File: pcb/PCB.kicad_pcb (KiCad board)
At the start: 4 copper layers, 29.2 x 51.1 mm, 35 parts, among them J1 Conn_01x15, J2 USB_C_Receptacle_USB2.0, J3 Conn_01x15, J4 TC2030, J5 Conn_01x04, SW1 SW_Push, SW2 SW_Push, U1 SN65HVD230, U2 AMS1117-3.3, U3 STM32F103C8T6, Y1 8MHz

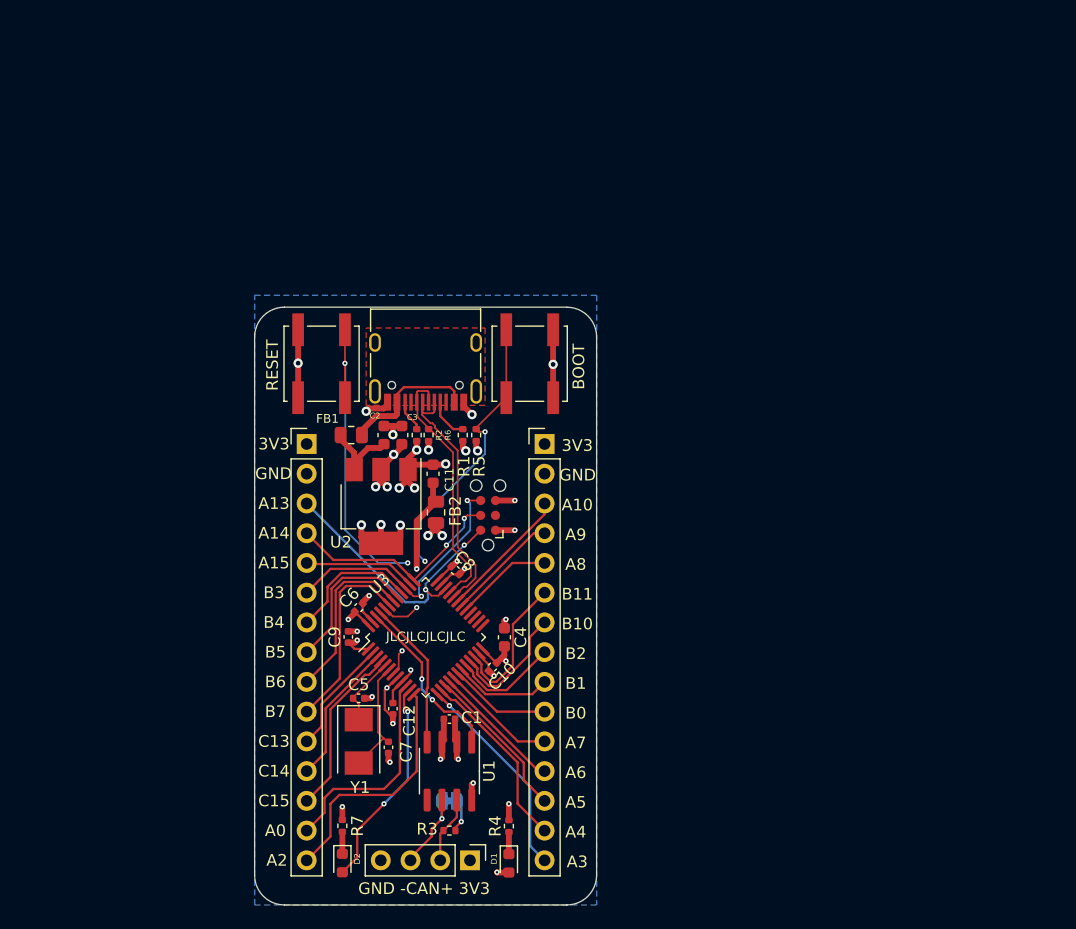
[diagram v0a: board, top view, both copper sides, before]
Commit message: created schematic and layout of the telemetry board
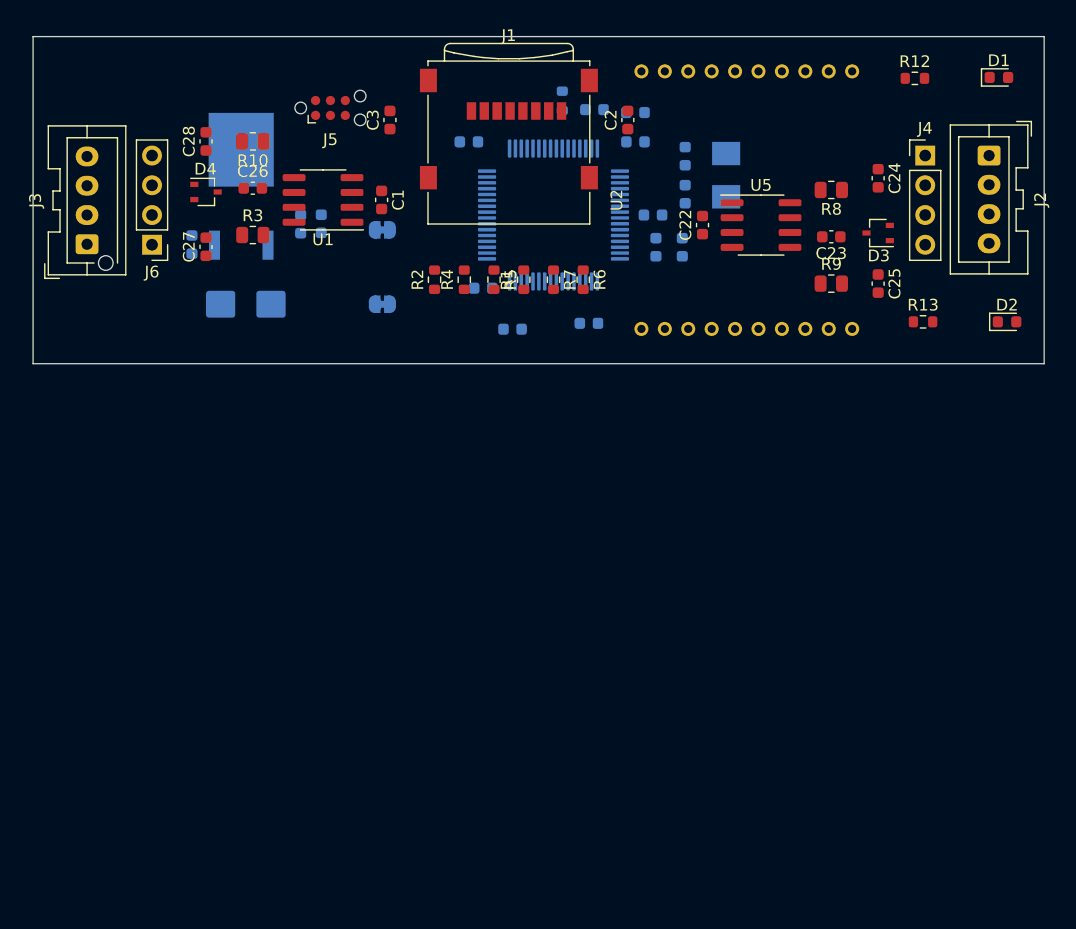
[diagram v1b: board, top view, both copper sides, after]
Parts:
- removed C10, C12, C8, C9: 100n, Capacitor_SMD:C_0402_1005Metric
- removed C11: 1u, Capacitor_SMD:C_0603_1608Metric
- removed C7: 30p, Capacitor_SMD:C_0402_1005Metric
- removed FB1, FB2: 100R@100MHz, Resistor_SMD:R_0805_2012Metric
- removed SW1, SW2: SW_Push, Button_Switch_SMD:SW_Push_1P1T_NO_CK_KSC7xxJ
- removed U3: STM32F103C8T6, Package_QFP:LQFP-48_7x7mm_P0.5mm
- removed Y1: 8MHz, Crystal:Crystal_SMD_5032-2Pin_5.0x3.2mm
- added C13: 4u7, Capacitor_SMD:C_0603_1608Metric, B.Cu at (169.2, 72.1)
- added C14: 100n, Capacitor_SMD:C_0603_1608Metric, B.Cu at (167.0, 72.1)
- added C15: 100n, Capacitor_SMD:C_0603_1608Metric, B.Cu at (161.7, 60.3)
- added C16: 100n, Capacitor_SMD:C_0603_1608Metric, B.Cu at (151.0, 63.1)
- added C17: 100n, Capacitor_SMD:C_0603_1608Metric, B.Cu at (165.2, 63.1)
- added C18: 1u, Capacitor_SMD:C_0603_1608Metric, B.Cu at (165.2, 60.6)
- added C19: 100n, Capacitor_SMD:C_0603_1608Metric, B.Cu at (154.7, 79.1)
- added C20: 4u7, Capacitor_SMD:C_0603_1608Metric, B.Cu at (152.2, 75.6)
- added C21: 100n, Capacitor_SMD:C_0603_1608Metric, B.Cu at (161.3, 78.6)
- added C22: 100n, Capacitor_SMD:C_0603_1608Metric, F.Cu at (171.0, 70.2)
- added C23: 100n, Capacitor_SMD:C_0603_1608Metric, F.Cu at (182.0, 71.2)
- added C24: 30p, Capacitor_SMD:C_0603_1608Metric, F.Cu at (186.0, 66.2)
- added C25: 30p, Capacitor_SMD:C_0603_1608Metric, F.Cu at (186.0, 75.2)
- added C26: 100n, Capacitor_SMD:C_0603_1608Metric, F.Cu at (132.6, 67.1)
- added C27: 30p, Capacitor_SMD:C_0603_1608Metric, F.Cu at (128.6, 72.1)
- added C28: 30p, Capacitor_SMD:C_0603_1608Metric, F.Cu at (128.6, 63.1)
- added C29: 30p, Capacitor_SMD:C_0603_1608Metric, B.Cu at (169.5, 64.3)
- added C30: 30p, Capacitor_SMD:C_0603_1608Metric, B.Cu at (169.5, 67.6)
- added C31: 100n, Capacitor_SMD:C_0603_1608Metric, B.Cu at (166.7, 69.3)
- added CR1: LF33CDT-TR, LF33CDT:DPAK_STM, B.Cu at (131.6, 65.5)
- added D3: D_TVS_Dual_AAC, Package_TO_SOT_SMD:SOT-323_SC-70, F.Cu at (186.0, 70.9)
- added D4: D_TVS_Dual_AAC, Package_TO_SOT_SMD:SOT-323_SC-70, F.Cu at (128.6, 67.4)
- added D5: SSB43L, Diode_SMD:D_SMB, B.Cu at (132.0, 77.0)
- added J6: 0.1 INCH HEADER, Connector_PinHeader_2.54mm:PinHeader_1x04_P2.54mm_Vertical, F.Cu at (124.0, 71.9)
- added JP2: SolderJumper_2_Bridged, Jumper:SolderJumper-2_P1.3mm_Bridged_RoundedPad1.0x1.5mm, B.Cu at (143.6, 70.6)
- added R10: 60, Resistor_SMD:R_0805_2012Metric, F.Cu at (132.6, 63.1)
- added R11: 33K, Resistor_SMD:R_0603_1608Metric, B.Cu at (159.0, 59.6)
- added R12: 1k, Resistor_SMD:R_0603_1608Metric, F.Cu at (189.1, 57.7)
- added R13: 1k, Resistor_SMD:R_0603_1608Metric, F.Cu at (189.8, 78.5)
- added R8: 60, Resistor_SMD:R_0805_2012Metric, F.Cu at (182.0, 67.2)
- added R9: 60, Resistor_SMD:R_0805_2012Metric, F.Cu at (182.0, 75.2)
- added U4: STM32F412RETx, Package_QFP:LQFP-64_10x10mm_P0.5mm, B.Cu at (158.2, 69.3)
- added U5: SN65HVD230, Package_SO:SOIC-8_3.9x4.9mm_P1.27mm, F.Cu at (176.0, 70.2)
- added Y2: 8MHz, Crystal:Crystal_SMD_5032-2Pin_5.0x3.2mm, B.Cu at (173.0, 65.9)
- C1: footprint Capacitor_SMD:C_0402_1005Metric -> Capacitor_SMD:C_0603_1608Metric
- C2: value 1u -> 4u7
- C3: value 1u -> 100n
- C4: moved to B.Cu
- C5: value 30p -> 4u7; footprint Capacitor_SMD:C_0402_1005Metric -> Capacitor_SMD:C_0603_1608Metric; moved to B.Cu
- C6: footprint Capacitor_SMD:C_0402_1005Metric -> Capacitor_SMD:C_0603_1608Metric; moved to B.Cu
- D1: value YELLOW -> LED
- D2: value BLUE -> LED
- J1: value Conn_01x15 -> Micro_SD_Card; footprint Connector_PinHeader_2.54mm:PinHeader_1x15_P2.54mm_Vertical -> Connector_Card:microSD_HC_Wuerth_693072010801
- J2: value USB_C_Receptacle_USB2.0 -> JST B04b-XASK; footprint Connector_USB:USB_C_Receptacle_HRO_TYPE-C-31-M-12 -> Connector_JST:JST_XA_B04B-XASK-1_1x04_P2.50mm_Vertical
- J3: value Conn_01x15 -> JST B04B-XASK; footprint Connector_PinHeader_2.54mm:PinHeader_1x15_P2.54mm_Vertical -> Connector_JST:JST_XA_B04B-XASK-1-A_1x04_P2.50mm_Vertical
- J4: value TC2030 -> 0.1 INCH HEADER; footprint Connector:Tag-Connect_TC2030-IDC-NL_2x03_P1.27mm_Vertical -> Connector_PinHeader_2.54mm:PinHeader_1x04_P2.54mm_Vertical
- J5: value Conn_01x04 -> TC2030; footprint Connector_PinHeader_2.54mm:PinHeader_1x04_P2.54mm_Vertical -> Connector:Tag-Connect_TC2030-IDC-NL_2x03_P1.27mm_Vertical
- JP1: value SolderJumper_Bridged -> SolderJumper_2_Bridged
- R1, R2, R5: value 5k1 -> 47k; footprint Resistor_SMD:R_0402_1005Metric -> Resistor_SMD:R_0603_1608Metric
- R3: value 120R -> 60; footprint Resistor_SMD:R_0402_1005Metric -> Resistor_SMD:R_0805_2012Metric
- R4, R6, R7: value 1k5 -> 47k; footprint Resistor_SMD:R_0402_1005Metric -> Resistor_SMD:R_0603_1608Metric
- U2: value AMS1117-3.3 -> XBPRO-900; footprint Package_TO_SOT_SMD:SOT-223-3_TabPin2 -> XBEE:XBEEPRO900HP
- moved D1 79.1 mm to (196.3, 57.6), turned to 0 degrees
- moved D2 73.2 mm to (197.0, 78.5), turned to 0 degrees
- moved J5 65.4 mm to (139.2, 60.2), turned to 0 degrees
- moved R3 53.6 mm to (132.6, 71.1)
- moved J2 51.0 mm to (195.4, 64.3), turned to -90 degrees
- moved R7 50.0 mm to (158.2, 74.9), turned to -90 degrees
- moved U1 50.0 mm to (138.6, 68.1), turned to 180 degrees
- moved J4 48.4 mm to (190.0, 64.3), turned to 0 degrees
- moved R4 46.8 mm to (150.6, 74.9)
- moved C1 44.7 mm to (143.6, 68.1), turned to -90 degrees
- moved C4 42.9 mm to (127.4, 71.9), turned to -90 degrees
- moved JP1 42.8 mm to (143.6, 77.0), turned to 180 degrees
- moved J3 42.6 mm to (118.4, 71.8), turned to 90 degrees
- moved U2 40.7 mm to (174.8, 68.1), turned to 0 degrees
- moved C5 40.7 mm to (138.4, 70.1), turned to 90 degrees
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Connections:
- C2 pad 1: VCC -> +3V3
- C4 pad 1: +3V3 -> GND
- C4 pad 2: GND -> +3V3
- C5 pad 1: /HSE_OUT -> Net-(CR1-IN)
- C6 pad 1: +3V3 -> GND
- C6 pad 2: GND -> Net-(CR1-IN)
- D1 pad 1: Net-(D1-Pad1) -> GND
- D1 pad 2: +3V3 -> Net-(D1-A)
- D2 pad 1: Net-(D2-Pad1) -> GND
- D2 pad 2: /LED_STAT -> Net-(D2-A)
- J1 pad 1: +3V3 -> SD-DAT2
- J1 pad 2: GND -> SD-DAT3
- J1 pad 3: SWDIO -> SD-CMD
- J1 pad 4: SWCLK -> +3V3
- J1 pad 5: PA15 -> SD-CLK
- J1 pad 6: SWO -> GND
- J1 pad 7: PB4 -> SD-DAT0
- J1 pad 8: PB5 -> SD-DAT1
- J1 pad 9: PB6 -> GND
- J3 pad 1: +3V3 -> +12V
- J3 pad 3: PA10 -> CAN2+
- J3 pad 4: PA9 -> CAN2-
- J4 pad 1: +3V3 -> +12V
- J4 pad 2: SWDIO -> GND
- J4 pad 3: unconnected-(J4-Pad3) -> CAN1+
- J4 pad 4: SWCLK -> CAN1-
- J5 pad 2: /CAN+ -> SWDIO
- J5 pad 3: /CAN- -> unconnected-(J5-nRESET-Pad3)
- J5 pad 4: GND -> SWCLK
- JP1 pad 1: /CAN- -> Net-(JP1-A)
- JP1 pad 2: Net-(JP1-Pad2) -> UART-RX
- R1 pad 1: Net-(J2-PadA5) -> +3V3
- R1 pad 2: GND -> SD-DAT2
- R2 pad 1: GND -> +3V3
- R2 pad 2: Net-(J2-PadB5) -> SD-DAT3
- R3 pad 1: /CAN+ -> CAN2+
- R3 pad 2: Net-(JP1-Pad2) -> Net-(U1-Vref)
- R4 pad 1: Net-(D1-Pad1) -> +3V3
- R4 pad 2: GND -> SD-CMD
- R5 pad 1: /BOOT0 -> SD-CLK
- R5 pad 2: GND -> +3V3
- R6 pad 1: +3V3 -> SD-DAT0
- R6 pad 2: USB_D+ -> +3V3
- R7 pad 1: Net-(D2-Pad1) -> SD-DAT1
- R7 pad 2: GND -> +3V3
- U1 pad 1: CANTX -> /Can Transceiver1/CANTX
- U1 pad 4: CANRX -> /Can Transceiver1/CANRX
- U1 pad 5: unconnected-(U1-Pad5) -> Net-(U1-Vref)
- U1 pad 6: /CAN- -> CAN2-
- U1 pad 7: /CAN+ -> CAN2+
- U2 pad 1: GND -> +3V3
- U2 pad 2: +3V3 -> Net-(JP1-A)
- U2 pad 3: VCC -> Net-(JP2-A)
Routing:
- net +3V3: track 44.0 -> 0.00 mm, vias 18 -> 0
- net GND: track 41.4 -> 0.00 mm, vias 23 -> 0
- net /NRST: track 35.9 -> 0.00 mm, vias 3 -> 0
- net /BOOT0: track 31.5 -> 0.00 mm, vias 3 -> 0
- net SWDIO: track 24.1 -> 0.00 mm, vias 2 -> 0
- net SWO: track 22.9 -> 0.00 mm, vias 2 -> 0
- net USB_D-: track 21.7 -> 0.00 mm
- net USB_D+: track 21.3 -> 0.00 mm
- net PA2: track 20.8 -> 0.00 mm
- net +3.3VA: track 20.2 -> 0.00 mm, vias 2 -> 0
- net SWCLK: track 19.4 -> 0.00 mm, vias 2 -> 0
- net PA0: track 18.4 -> 0.00 mm
- net /LED_STAT: track 18.2 -> 0.00 mm, vias 2 -> 0
- net PA3: track 18.0 -> 0.00 mm, vias 1 -> 0
- net PB7: track 16.5 -> 0.00 mm
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- removed copper zone on B.Cu, net GND
- removed copper zone on F.Cu, net unconnected-(J2-PadS1)
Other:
- board size 29.2 x 51.1 mm -> 86.4 x 27.9 mm
- board text removed: "3V3"
- board text removed: "3V3 +CAN- GND"
- board text removed: "A0"
- board text removed: "A10"
- board text removed: "A13"
- board text removed: "A14"
- board text removed: "A15"
- board text removed: "A2"
- board text removed: "A3"
- board text removed: "A4"
- board text removed: "A5"
- board text removed: "A6"
- board text removed: "A7"
- board text removed: "A8"
- board text removed: "A9"
- board text removed: "B0"
- board text removed: "B1"
- board text removed: "B10"
- board text removed: "B11"
- board text removed: "B2"
- board text removed: "B3"
- board text removed: "B4"
- board text removed: "B5"
- board text removed: "B6"
- board text removed: "B7"
- board text removed: "BOOT"
- board text removed: "C13"
- board text removed: "C14"
- board text removed: "C15"
- board text removed: "CAN TERM"
- board text removed: "GND"
- board text removed: "GND -CAN+ 3V3"
- board text removed: "JLCJLCJLCJLC"
- board text removed: "RESET"
- board text removed: "Rev 1"
- board text removed: "STM32F103 CAN/USB-C Jack LeFevre July 2022"
- board text removed: "SWCLK"
- board text removed: "SWDIO"
- board text removed: "SWO"

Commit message: Finished Telemetry PCB
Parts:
- added G***: LOGO, toucan:toucan, B.Cu at (182.0, 70.4)
- moved D2 6.93 mm to (190.1, 78.9)
- moved R13 6.72 mm to (196.5, 78.8)
- moved R2 5.36 mm to (153.4, 74.2)
- moved JP2 5.10 mm to (143.4, 75.7), turned to 90 degrees
- moved R4 4.85 mm to (155.4, 74.2)
- moved R5 4.53 mm to (157.6, 74.1)
- moved R1 4.49 mm to (151.3, 74.2)
- moved JP1 3.77 mm to (147.2, 75.7), turned to 90 degrees
- moved R7 3.40 mm to (161.6, 74.2)
- moved R6 1.39 mm to (159.6, 74.2)
- moved R12 0.94 mm to (190.0, 57.6), turned to 180 degrees
- turned D1 to 180 degrees
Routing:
- net +12V: track 0.00 -> 108.9 mm
- net +3V3: track 0.00 -> 100.6 mm, vias 0 -> 13
- net GND: track 0.00 -> 71.7 mm, vias 0 -> 37
- net MICROLED: track 0.00 -> 56.4 mm, vias 0 -> 1
- net SD-CMD: track 0.00 -> 32.0 mm, vias 0 -> 1
- net Net-(JP2-A): track 0.00 -> 29.9 mm
- net Net-(JP1-A): track 0.00 -> 29.4 mm
- net SD-DAT1: track 0.00 -> 28.5 mm, vias 0 -> 1
- net CAN2-: track 0.00 -> 28.4 mm
- net CAN1-: track 0.00 -> 28.2 mm
- net SD-DAT0: track 0.00 -> 27.8 mm, vias 0 -> 1
- net SD-CLK: track 0.00 -> 27.0 mm, vias 0 -> 1
- net SWO: track 0.00 -> 25.8 mm, vias 0 -> 1
- net CAN2+: track 0.00 -> 25.8 mm
- net UART-RX: track 0.00 -> 24.1 mm
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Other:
- board size 86.4 x 27.9 mm -> 86.4 x 28 mm
- board text added: "12V"
- board text added: "CAN1+"
- board text added: "CAN1-"
- board text added: "CAN2+"
- board text added: "CAN2-"
- board text added: "GND"
- board text added: "Leo Lake Bronco Racing Telemetry Board Rev 2 JAN 2024"
- board text added: "RX"
- board text added: "TX"
